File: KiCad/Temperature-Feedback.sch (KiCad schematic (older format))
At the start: 8 parts, among them U3 MCP9700A, U4 MCP617

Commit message: controller board schematic complete
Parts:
- gave numbers to parts that had none: 6
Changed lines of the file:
@@
 $Descr A4 11693 8268
 encoding utf-8
-Sheet 2 5
+Sheet 2 6
 Title ""
 Date ""
@@
 $EndComp
 $Comp
-L +5V #PWR?
+L +5V #PWR18
 U 1 1 564E7633
 P 5900 3500
-F 0 "#PWR?" H 5900 3350 50  0001 C CNN
+F 0 "#PWR18" H 5900 3350 50  0001 C CNN
 F 1 "+5V" H 5900 3640 50  0000 C CNN
 F 2 "" H 5900 3500 60  0000 C CNN
@@
 $EndComp
 $Comp
-L GND #PWR?
+L GND #PWR19
 U 1 1 564E76F6
 P 5900 4300
-F 0 "#PWR?" H 5900 4050 50  0001 C CNN
+F 0 "#PWR19" H 5900 4050 50  0001 C CNN
 F 1 "GND" H 5900 4150 50  0000 C CNN
 F 2 "" H 5900 4300 60  0000 C CNN
@@
 K+
 $Comp
-L MCP41050 U?
+L MCP41050 U2
 U 1 1 567EB0B4
 P 4450 3050
-F 0 "U?" H 4450 3400 60  0000 C CNN
+F 0 "U2" H 4450 3400 60  0000 C CNN
 F 1 "MCP41050" H 4450 2700 60  0000 C CNN
 F 2 "" H 4450 3050 60  0000 C CNN
@@
 Vref-
 $Comp
-L +5V #PWR?
+L +5V #PWR16
 U 1 1 567EB483
 P 5900 1700
-F 0 "#PWR?" H 5900 1550 50  0001 C CNN
+F 0 "#PWR16" H 5900 1550 50  0001 C CNN
 F 1 "+5V" H 5900 1840 50  0000 C CNN
 F 2 "" H 5900 1700 50  0000 C CNN
@@
 $EndComp
 $Comp
-L +5V #PWR?
+L +5V #PWR22
 U 1 1 567EB4D3
 P 8700 3250
-F 0 "#PWR?" H 8700 3100 50  0001 C CNN
+F 0 "#PWR22" H 8700 3100 50  0001 C CNN
 F 1 "+5V" H 8700 3390 50  0000 C CNN
 F 2 "" H 8700 3250 50  0000 C CNN
@@
 $EndComp
 $Comp
-L +5V #PWR?
+L +5V #PWR15
 U 1 1 567EB513
 P 4900 2750
-F 0 "#PWR?" H 4900 2600 50  0001 C CNN
+F 0 "#PWR15" H 4900 2600 50  0001 C CNN
 F 1 "+5V" H 4900 2890 50  0000 C CNN
 F 2 "" H 4900 2750 50  0000 C CNN
@@
 NoConn ~ 4900 3200
 $Comp
-L R R?
+L R R19
 U 1 1 567EB65C
 P 7700 4850
-F 0 "R?" V 7780 4850 50  0000 C CNN
+F 0 "R19" V 7780 4850 50  0000 C CNN
 F 1 "R" V 7700 4850 50  0000 C CNN
 F 2 "" V 7630 4850 50  0000 C CNN
@@
 $EndComp
 $Comp
-L R R?
+L R R20
 U 1 1 567EB832
 P 7700 5350
-F 0 "R?" V 7780 5350 50  0000 C CNN
+F 0 "R20" V 7780 5350 50  0000 C CNN
 F 1 "R" V 7700 5350 50  0000 C CNN
 F 2 "" V 7630 5350 50  0000 C CNN
@@
 $EndComp
 $Comp
-L +5V #PWR?
+L +5V #PWR20
 U 1 1 567EB9AA
 P 7700 4600
-F 0 "#PWR?" H 7700 4450 50  0001 C CNN
+F 0 "#PWR20" H 7700 4450 50  0001 C CNN
 F 1 "+5V" H 7700 4740 50  0000 C CNN
 F 2 "" H 7700 4600 50  0000 C CNN
@@
 $EndComp
 $Comp
-L GND #PWR?
+L GND #PWR21
 U 1 1 567EB9D6
 P 7700 5700
-F 0 "#PWR?" H 7700 5450 50  0001 C CNN
+F 0 "#PWR21" H 7700 5450 50  0001 C CNN
 F 1 "GND" H 7700 5550 50  0000 C CNN
 F 2 "" H 7700 5700 50  0000 C CNN
@@
 $EndComp
 $Comp
-L GND #PWR?
+L GND #PWR23
 U 1 1 567EB9F6
 P 8700 4350
-F 0 "#PWR?" H 8700 4100 50  0001 C CNN
+F 0 "#PWR23" H 8700 4100 50  0001 C CNN
 F 1 "GND" H 8700 4200 50  0000 C CNN
 F 2 "" H 8700 4350 50  0000 C CNN
@@
 $EndComp
 $Comp
-L GND #PWR?
+L GND #PWR17
 U 1 1 567EBA46
 P 5900 2500
-F 0 "#PWR?" H 5900 2250 50  0001 C CNN
+F 0 "#PWR17" H 5900 2250 50  0001 C CNN
 F 1 "GND" H 5900 2350 50  0000 C CNN
 F 2 "" H 5900 2500 50  0000 C CNN
@@
 $EndComp
 $Comp
-L GND #PWR?
+L GND #PWR14
 U 1 1 567EBA84
 P 4000 3400
-F 0 "#PWR?" H 4000 3150 50  0001 C CNN
+F 0 "#PWR14" H 4000 3150 50  0001 C CNN
 F 1 "GND" H 4000 3250 50  0000 C CNN
 F 2 "" H 4000 3400 50  0000 C CNN
@@
 $EndComp
 $Comp
-L R R?
+L R R16
 U 1 1 567EBBB8
 P 5900 4700
-F 0 "R?" V 5980 4700 50  0000 C CNN
+F 0 "R16" V 5980 4700 50  0000 C CNN
 F 1 "R" V 5900 4700 50  0000 C CNN
 F 2 "" V 5830 4700 50  0000 C CNN
@@
 $EndComp
 $Comp
-L R R?
+L R R18
 U 1 1 567EBC11
 P 6750 4700
-F 0 "R?" V 6830 4700 50  0000 C CNN
+F 0 "R18" V 6830 4700 50  0000 C CNN
 F 1 "R" V 6750 4700 50  0000 C CNN
 F 2 "" V 6680 4700 50  0000 C CNN
@@
 $EndComp
 $Comp
-L R R?
+L R R17
 U 1 1 567EBCDE
 P 6750 3100
-F 0 "R?" V 6830 3100 50  0000 C CNN
+F 0 "R17" V 6830 3100 50  0000 C CNN
 F 1 "R" V 6750 3100 50  0000 C CNN
 F 2 "" V 6680 3100 50  0000 C CNN

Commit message: HeatOn fix, replaced R1-8 with array
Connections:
- net labels added: VDD
- net labels removed: +5V
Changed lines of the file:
@@
 F 0 "U4" H 5750 4100 60  0000 L CNN
 F 1 "MCP617" H 5750 3650 60  0000 L CNN
-F 2 "" H 5800 3900 60  0000 C CNN
+F 2 "" H 5800 3900 60  0001 C CNN
 F 3 "" H 5800 3900 60  0000 C CNN
 	1    5800 3900
@@
 F 0 "U4" H 5750 2300 60  0000 L CNN
 F 1 "MCP617" H 5750 1850 60  0000 L CNN
-F 2 "" H 5800 2100 60  0000 C CNN
+F 2 "" H 5800 2100 60  0001 C CNN
 F 3 "" H 5800 2100 60  0000 C CNN
 	2    5800 2100
@@
 $EndComp
 $Comp
-L +5V #PWR18
-U 1 1 564E7633
-P 5900 3500
-F 0 "#PWR18" H 5900 3350 50  0001 C CNN
-F 1 "+5V" H 5900 3640 50  0000 C CNN
-F 2 "" H 5900 3500 60  0000 C CNN
-F 3 "" H 5900 3500 60  0000 C CNN
-	1    5900 3500
-	1    0    0    -1
-$EndComp
-$Comp
-L GND #PWR19
+L GND #PWR014
 U 1 1 564E76F6
 P 5900 4300
-F 0 "#PWR19" H 5900 4050 50  0001 C CNN
+F 0 "#PWR014" H 5900 4050 50  0001 C CNN
 F 1 "GND" H 5900 4150 50  0000 C CNN
 F 2 "" H 5900 4300 60  0000 C CNN
@@
 Text HLabel 2500 2100 0    60   Output ~ 0
 Tk
-$Comp
-L MCP9700A U3
-U 1 1 564E89FE
-P 8700 3800
-F 0 "U3" H 8950 3800 60  0000 L CNN
-F 1 "MCP9700A" H 8950 3700 60  0000 L CNN
-F 2 "" H 8700 3800 60  0000 C CNN
-F 3 "" H 8700 3800 60  0000 C CNN
-	1    8700 3800
-	1    0    0    -1
-$EndComp
 Text Notes 9000 3550 0    60   ~ 0
 Cold Junction Temperature Sensor\n(place as close as possible to terminals)
@@
 F 0 "U2" H 4450 3400 60  0000 C CNN
 F 1 "MCP41050" H 4450 2700 60  0000 C CNN
-F 2 "" H 4450 3050 60  0000 C CNN
+F 2 "" H 4450 3050 60  0001 C CNN
 F 3 "" H 4450 3050 60  0000 C CNN
 	1    4450 3050
@@
 Text HLabel 2500 5100 0    60   Output ~ 0
 Vref-
-$Comp
-L +5V #PWR16
-U 1 1 567EB483
-P 5900 1700
-F 0 "#PWR16" H 5900 1550 50  0001 C CNN
-F 1 "+5V" H 5900 1840 50  0000 C CNN
-F 2 "" H 5900 1700 50  0000 C CNN
-F 3 "" H 5900 1700 50  0000 C CNN
-	1    5900 1700
-	1    0    0    -1
-$EndComp
-$Comp
-L +5V #PWR22
-U 1 1 567EB4D3
-P 8700 3250
-F 0 "#PWR22" H 8700 3100 50  0001 C CNN
-F 1 "+5V" H 8700 3390 50  0000 C CNN
-F 2 "" H 8700 3250 50  0000 C CNN
-F 3 "" H 8700 3250 50  0000 C CNN
-	1    8700 3250
-	1    0    0    -1
-$EndComp
-$Comp
-L +5V #PWR15
-U 1 1 567EB513
-P 4900 2750
-F 0 "#PWR15" H 4900 2600 50  0001 C CNN
-F 1 "+5V" H 4900 2890 50  0000 C CNN
-F 2 "" H 4900 2750 50  0000 C CNN
-F 3 "" H 4900 2750 50  0000 C CNN
-	1    4900 2750
-	1    0    0    -1
-$EndComp
 NoConn ~ 4900 3200
 $Comp
@@
 F 0 "R19" V 7780 4850 50  0000 C CNN
 F 1 "R" V 7700 4850 50  0000 C CNN
-F 2 "" V 7630 4850 50  0000 C CNN
+F 2 "" V 7630 4850 50  0001 C CNN
 F 3 "" H 7700 4850 50  0000 C CNN
 	1    7700 4850
@@
 F 0 "R20" V 7780 5350 50  0000 C CNN
 F 1 "R" V 7700 5350 50  0000 C CNN
-F 2 "" V 7630 5350 50  0000 C CNN
+F 2 "" V 7630 5350 50  0001 C CNN
 F 3 "" H 7700 5350 50  0000 C CNN
 	1    7700 5350
@@
 $EndComp
 $Comp
-L +5V #PWR20
-U 1 1 567EB9AA
-P 7700 4600
-F 0 "#PWR20" H 7700 4450 50  0001 C CNN
-F 1 "+5V" H 7700 4740 50  0000 C CNN
-F 2 "" H 7700 4600 50  0000 C CNN
-F 3 "" H 7700 4600 50  0000 C CNN
-	1    7700 4600
-	1    0    0    -1
-$EndComp
-$Comp
-L GND #PWR21
+L GND #PWR015
 U 1 1 567EB9D6
 P 7700 5700
-F 0 "#PWR21" H 7700 5450 50  0001 C CNN
+F 0 "#PWR015" H 7700 5450 50  0001 C CNN
 F 1 "GND" H 7700 5550 50  0000 C CNN
 F 2 "" H 7700 5700 50  0000 C CNN
@@
 $EndComp
 $Comp
-L GND #PWR23
+L GND #PWR016
 U 1 1 567EB9F6
 P 8700 4350
-F 0 "#PWR23" H 8700 4100 50  0001 C CNN
+F 0 "#PWR016" H 8700 4100 50  0001 C CNN
 F 1 "GND" H 8700 4200 50  0000 C CNN
 F 2 "" H 8700 4350 50  0000 C CNN
@@
 $EndComp
 $Comp
-L GND #PWR17
+L GND #PWR017
 U 1 1 567EBA46
 P 5900 2500
-F 0 "#PWR17" H 5900 2250 50  0001 C CNN
+F 0 "#PWR017" H 5900 2250 50  0001 C CNN
 F 1 "GND" H 5900 2350 50  0000 C CNN
 F 2 "" H 5900 2500 50  0000 C CNN
@@
 $EndComp
 $Comp
-L GND #PWR14
+L GND #PWR018
 U 1 1 567EBA84
 P 4000 3400
-F 0 "#PWR14" H 4000 3150 50  0001 C CNN
+F 0 "#PWR018" H 4000 3150 50  0001 C CNN
 F 1 "GND" H 4000 3250 50  0000 C CNN
 F 2 "" H 4000 3400 50  0000 C CNN
@@
 F 0 "R16" V 5980 4700 50  0000 C CNN
 F 1 "R" V 5900 4700 50  0000 C CNN
-F 2 "" V 5830 4700 50  0000 C CNN
+F 2 "" V 5830 4700 50  0001 C CNN
 F 3 "" H 5900 4700 50  0000 C CNN
 	1    5900 4700
@@
 F 0 "R18" V 6830 4700 50  0000 C CNN
 F 1 "R" V 6750 4700 50  0000 C CNN
-F 2 "" V 6680 4700 50  0000 C CNN
+F 2 "" V 6680 4700 50  0001 C CNN
 F 3 "" H 6750 4700 50  0000 C CNN
 	1    6750 4700
@@
 F 0 "R17" V 6830 3100 50  0000 C CNN
 F 1 "R" V 6750 3100 50  0000 C CNN
-F 2 "" V 6680 3100 50  0000 C CNN
+F 2 "" V 6680 3100 50  0001 C CNN
 F 3 "" H 6750 3100 50  0000 C CNN
 	1    6750 3100
@@
 Wire Wire Line
 	4000 3200 4000 3400
-Wire Wire Line
-	7700 4600 7700 4700
 Wire Wire Line
 	7700 5500 7700 5700
@@
 Wire Wire Line
 	2500 3100 4000 3100
+$Comp
+L MCP9700A U3
+U 1 1 5682CB9B
+P 8700 3800
+F 0 "U3" H 8950 3800 60  0000 L CNN
+F 1 "MCP9700A" H 8950 3700 60  0000 L CNN
+F 2 "" H 8700 3800 60  0001 C CNN
+F 3 "" H 8700 3800 60  0000 C CNN
+	1    8700 3800
+	1    0    0    -1
+$EndComp
+Wire Wire Line
+	7700 4600 7700 4700
+$Comp
+L VDD #PWR019
+U 1 1 5682D8FB
+P 7700 4600
+F 0 "#PWR019" H 7700 4450 50  0001 C CNN
+F 1 "VDD" H 7700 4750 50  0000 C CNN
+F 2 "" H 7700 4600 50  0000 C CNN
+F 3 "" H 7700 4600 50  0000 C CNN
+	1    7700 4600
+	1    0    0    -1
+$EndComp
+$Comp
+L VDD #PWR020
+U 1 1 5682DBD5
+P 8700 3250
+F 0 "#PWR020" H 8700 3100 50  0001 C CNN
+F 1 "VDD" H 8700 3400 50  0000 C CNN
+F 2 "" H 8700 3250 50  0000 C CNN
+F 3 "" H 8700 3250 50  0000 C CNN
+	1    8700 3250
+	1    0    0    -1
+$EndComp
+$Comp
+L VDD #PWR021
+U 1 1 5682DC73
+P 5900 1700
+F 0 "#PWR021" H 5900 1550 50  0001 C CNN
+F 1 "VDD" H 5900 1850 50  0000 C CNN
+F 2 "" H 5900 1700 50  0000 C CNN
+F 3 "" H 5900 1700 50  0000 C CNN
+	1    5900 1700
+	1    0    0    -1
+$EndComp
+$Comp
+L VDD #PWR022
+U 1 1 5682DD06
+P 4900 2750
+F 0 "#PWR022" H 4900 2600 50  0001 C CNN
+F 1 "VDD" H 4900 2900 50  0000 C CNN
+F 2 "" H 4900 2750 50  0000 C CNN
+F 3 "" H 4900 2750 50  0000 C CNN
+	1    4900 2750
+	1    0    0    -1
+$EndComp
+$Comp
+L VDD #PWR023
+U 1 1 5682DD77
+P 5900 3500
+F 0 "#PWR023" H 5900 3350 50  0001 C CNN
+F 1 "VDD" H 5900 3650 50  0000 C CNN
+F 2 "" H 5900 3500 50  0000 C CNN
+F 3 "" H 5900 3500 50  0000 C CNN
+	1    5900 3500
+	1    0    0    -1
+$EndComp
 $EndSCHEMATC

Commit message: kicad resistor package associations complete
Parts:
- R16, R17, R18, R19, R20: footprint (none) -> Resistors_ThroughHole:Resistor_Horizontal_RM10mm
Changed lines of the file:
@@
 F 0 "R19" V 7780 4850 50  0000 C CNN
 F 1 "R" V 7700 4850 50  0000 C CNN
-F 2 "" V 7630 4850 50  0001 C CNN
+F 2 "Resistors_ThroughHole:Resistor_Horizontal_RM10mm" V 7630 4850 50  0001 C CNN
 F 3 "" H 7700 4850 50  0000 C CNN
 	1    7700 4850
@@
 F 0 "R20" V 7780 5350 50  0000 C CNN
 F 1 "R" V 7700 5350 50  0000 C CNN
-F 2 "" V 7630 5350 50  0001 C CNN
+F 2 "Resistors_ThroughHole:Resistor_Horizontal_RM10mm" V 7630 5350 50  0001 C CNN
 F 3 "" H 7700 5350 50  0000 C CNN
 	1    7700 5350
@@
 F 0 "R16" V 5980 4700 50  0000 C CNN
 F 1 "R" V 5900 4700 50  0000 C CNN
-F 2 "" V 5830 4700 50  0001 C CNN
+F 2 "Resistors_ThroughHole:Resistor_Horizontal_RM10mm" V 5830 4700 50  0001 C CNN
 F 3 "" H 5900 4700 50  0000 C CNN
 	1    5900 4700
@@
 F 0 "R18" V 6830 4700 50  0000 C CNN
 F 1 "R" V 6750 4700 50  0000 C CNN
-F 2 "" V 6680 4700 50  0001 C CNN
+F 2 "Resistors_ThroughHole:Resistor_Horizontal_RM10mm" V 6680 4700 50  0001 C CNN
 F 3 "" H 6750 4700 50  0000 C CNN
 	1    6750 4700
@@
 F 0 "R17" V 6830 3100 50  0000 C CNN
 F 1 "R" V 6750 3100 50  0000 C CNN
-F 2 "" V 6680 3100 50  0001 C CNN
+F 2 "Resistors_ThroughHole:Resistor_Horizontal_RM10mm" V 6680 3100 50  0001 C CNN
 F 3 "" H 6750 3100 50  0000 C CNN
 	1    6750 3100

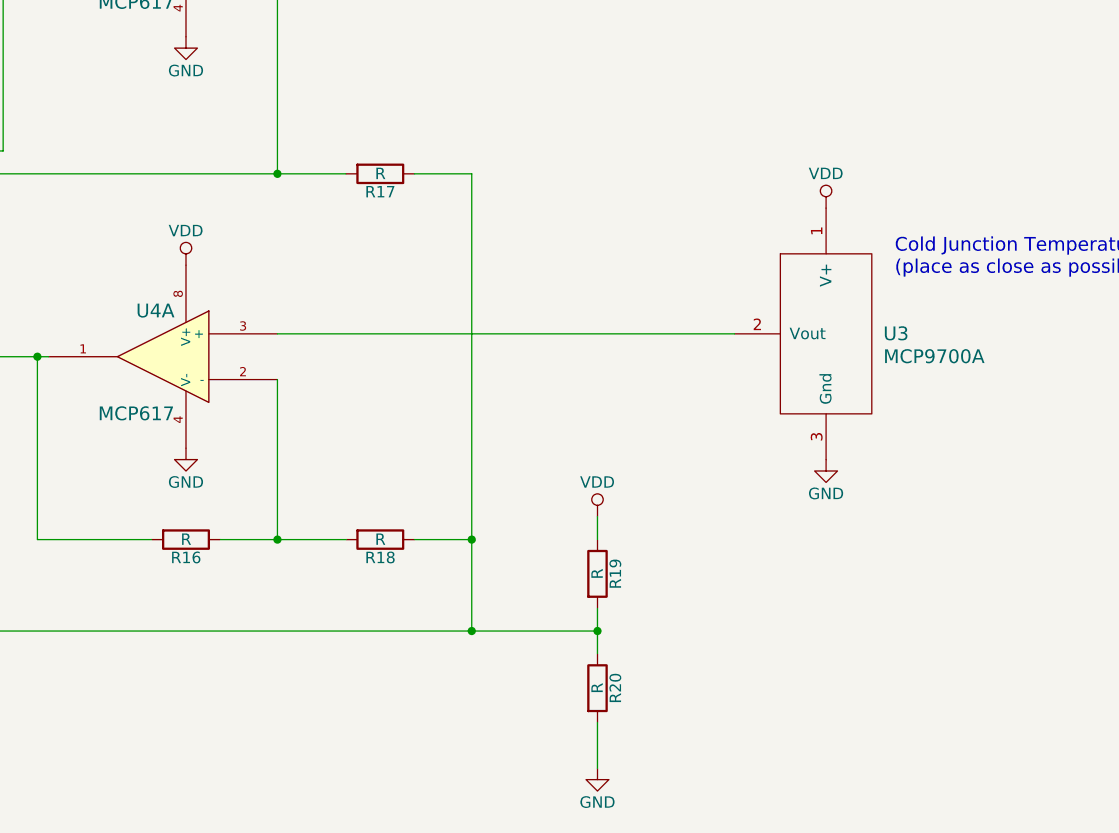
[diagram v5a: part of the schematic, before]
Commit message: temperature feedback resistor design
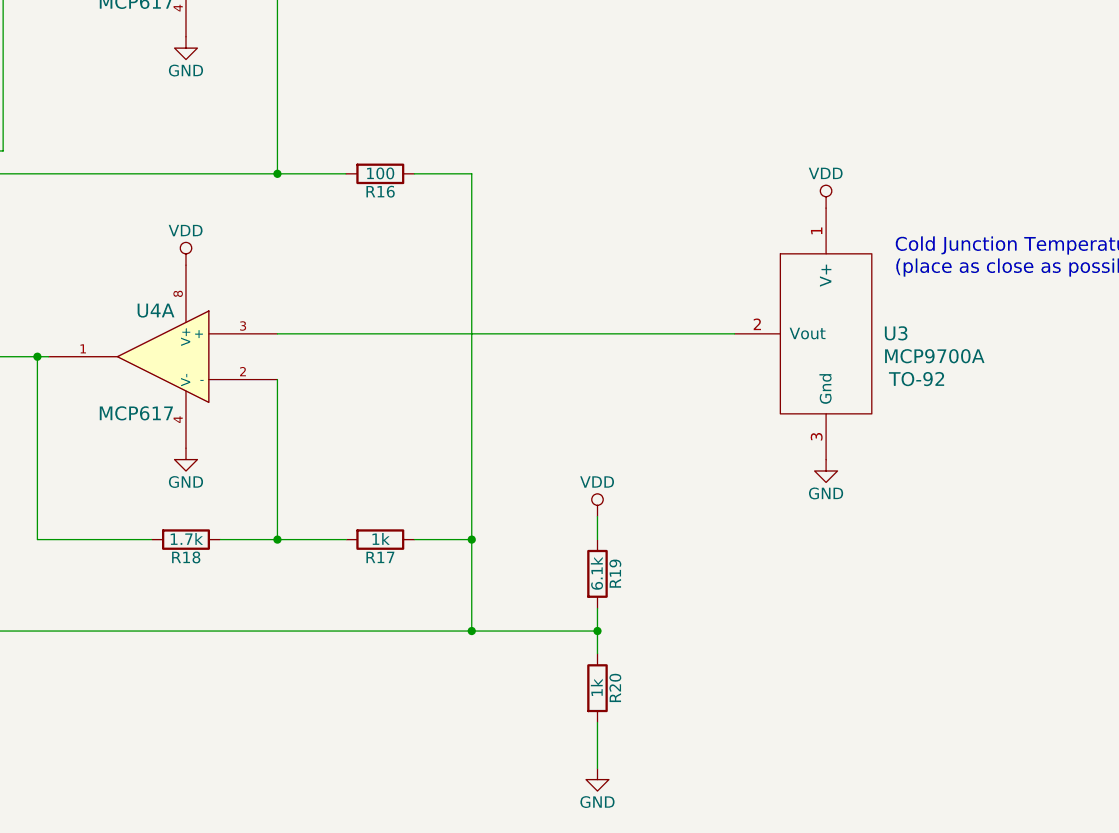
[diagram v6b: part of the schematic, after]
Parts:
- R16: renamed from R17; value R -> 100
- R17: renamed from R18; value R -> 1k
- R18: renamed from R16; value R -> 1.7k
- R19: value R -> 6.1k
- R20: value R -> 1k
- U3: footprint (none) -> TO-92
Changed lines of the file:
@@
 P 7700 4850
 F 0 "R19" V 7780 4850 50  0000 C CNN
-F 1 "R" V 7700 4850 50  0000 C CNN
+F 1 "6.1k" V 7700 4850 50  0000 C CNN
 F 2 "Resistors_ThroughHole:Resistor_Horizontal_RM10mm" V 7630 4850 50  0001 C CNN
 F 3 "" H 7700 4850 50  0000 C CNN
@@
 P 7700 5350
 F 0 "R20" V 7780 5350 50  0000 C CNN
-F 1 "R" V 7700 5350 50  0000 C CNN
+F 1 "1k" V 7700 5350 50  0000 C CNN
 F 2 "Resistors_ThroughHole:Resistor_Horizontal_RM10mm" V 7630 5350 50  0001 C CNN
 F 3 "" H 7700 5350 50  0000 C CNN
@@
 $EndComp
 $Comp
-L R R16
+L R R18
 U 1 1 567EBBB8
 P 5900 4700
-F 0 "R16" V 5980 4700 50  0000 C CNN
-F 1 "R" V 5900 4700 50  0000 C CNN
+F 0 "R18" V 5980 4700 50  0000 C CNN
+F 1 "1.7k" V 5900 4700 50  0000 C CNN
 F 2 "Resistors_ThroughHole:Resistor_Horizontal_RM10mm" V 5830 4700 50  0001 C CNN
 F 3 "" H 5900 4700 50  0000 C CNN
@@
 $EndComp
 $Comp
-L R R18
+L R R17
 U 1 1 567EBC11
 P 6750 4700
-F 0 "R18" V 6830 4700 50  0000 C CNN
-F 1 "R" V 6750 4700 50  0000 C CNN
+F 0 "R17" V 6830 4700 50  0000 C CNN
+F 1 "1k" V 6750 4700 50  0000 C CNN
 F 2 "Resistors_ThroughHole:Resistor_Horizontal_RM10mm" V 6680 4700 50  0001 C CNN
 F 3 "" H 6750 4700 50  0000 C CNN
@@
 $EndComp
 $Comp
-L R R17
+L R R16
 U 1 1 567EBCDE
 P 6750 3100
-F 0 "R17" V 6830 3100 50  0000 C CNN
-F 1 "R" V 6750 3100 50  0000 C CNN
+F 0 "R16" V 6830 3100 50  0000 C CNN
+F 1 "100" V 6750 3100 50  0000 C CNN
 F 2 "Resistors_ThroughHole:Resistor_Horizontal_RM10mm" V 6680 3100 50  0001 C CNN
 F 3 "" H 6750 3100 50  0000 C CNN
@@
 Wire Wire Line
 	2500 3100 4000 3100
-$Comp
-L MCP9700A U3
-U 1 1 5682CB9B
-P 8700 3800
-F 0 "U3" H 8950 3800 60  0000 L CNN
-F 1 "MCP9700A" H 8950 3700 60  0000 L CNN
-F 2 "" H 8700 3800 60  0001 C CNN
-F 3 "" H 8700 3800 60  0000 C CNN
-	1    8700 3800
-	1    0    0    -1
-$EndComp
 Wire Wire Line
 	7700 4600 7700 4700
@@
 	1    0    0    -1
 $EndComp
+$Comp
+L MCP9700A U3
+U 1 1 56880F29
+P 8700 3800
+F 0 "U3" H 8950 3800 60  0000 L CNN
+F 1 "MCP9700A" H 8950 3700 60  0000 L CNN
+F 2 "TO-92" H 9100 3600 60  0000 C CNN
+F 3 "" H 8700 3800 60  0000 C CNN
+	1    8700 3800
+	1    0    0    -1
+$EndComp

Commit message: IC BOM and footprints complete
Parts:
- U2, U4: footprint (none) -> Easy-PCB-footprints:DIP-8
- U4: renamed from U3; footprint TO-92 -> Easy-PCB-footprints:TO-92
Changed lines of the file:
@@
 P 5800 3900
 AR Path="/564E7160" Ref="U4"  Part="1"
-AR Path="/564E6B87/564E7160" Ref="U4"  Part="1"
-F 0 "U4" H 5750 4100 60  0000 L CNN
+AR Path="/564E6B87/564E7160" Ref="U3"  Part="1"
+F 0 "U3" H 5750 4100 60  0000 L CNN
 F 1 "MCP617" H 5750 3650 60  0000 L CNN
-F 2 "" H 5800 3900 60  0001 C CNN
+F 2 "Easy-PCB-footprints:DIP-8" H 5800 3900 60  0001 C CNN
 F 3 "" H 5800 3900 60  0000 C CNN
 	1    5800 3900
@@
 P 5800 2100
 AR Path="/564E743F" Ref="U4"  Part="2"
-AR Path="/564E6B87/564E743F" Ref="U4"  Part="2"
-F 0 "U4" H 5750 2300 60  0000 L CNN
+AR Path="/564E6B87/564E743F" Ref="U3"  Part="2"
+F 0 "U3" H 5750 2300 60  0000 L CNN
 F 1 "MCP617" H 5750 1850 60  0000 L CNN
-F 2 "" H 5800 2100 60  0001 C CNN
+F 2 "Easy-PCB-footprints:DIP-8" H 5800 2100 60  0001 C CNN
 F 3 "" H 5800 2100 60  0000 C CNN
 	2    5800 2100
@@
 F 0 "U2" H 4450 3400 60  0000 C CNN
 F 1 "MCP41050" H 4450 2700 60  0000 C CNN
-F 2 "" H 4450 3050 60  0001 C CNN
+F 2 "Easy-PCB-footprints:DIP-8" H 4450 3050 60  0001 C CNN
 F 3 "" H 4450 3050 60  0000 C CNN
 	1    4450 3050
@@
 $EndComp
 $Comp
-L MCP9700A U3
+L MCP9700A U4
 U 1 1 56880F29
 P 8700 3800
-F 0 "U3" H 8950 3800 60  0000 L CNN
+F 0 "U4" H 8950 3800 60  0000 L CNN
 F 1 "MCP9700A" H 8950 3700 60  0000 L CNN
-F 2 "TO-92" H 9100 3600 60  0000 C CNN
+F 2 "Easy-PCB-footprints:TO-92" H 9100 3600 60  0001 C CNN
 F 3 "" H 8700 3800 60  0000 C CNN
 	1    8700 3800
